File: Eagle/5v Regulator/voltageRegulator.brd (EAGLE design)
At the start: 49 x 43 mm, 9 parts, among them U1 LM2576HVS-5.0/NOPB

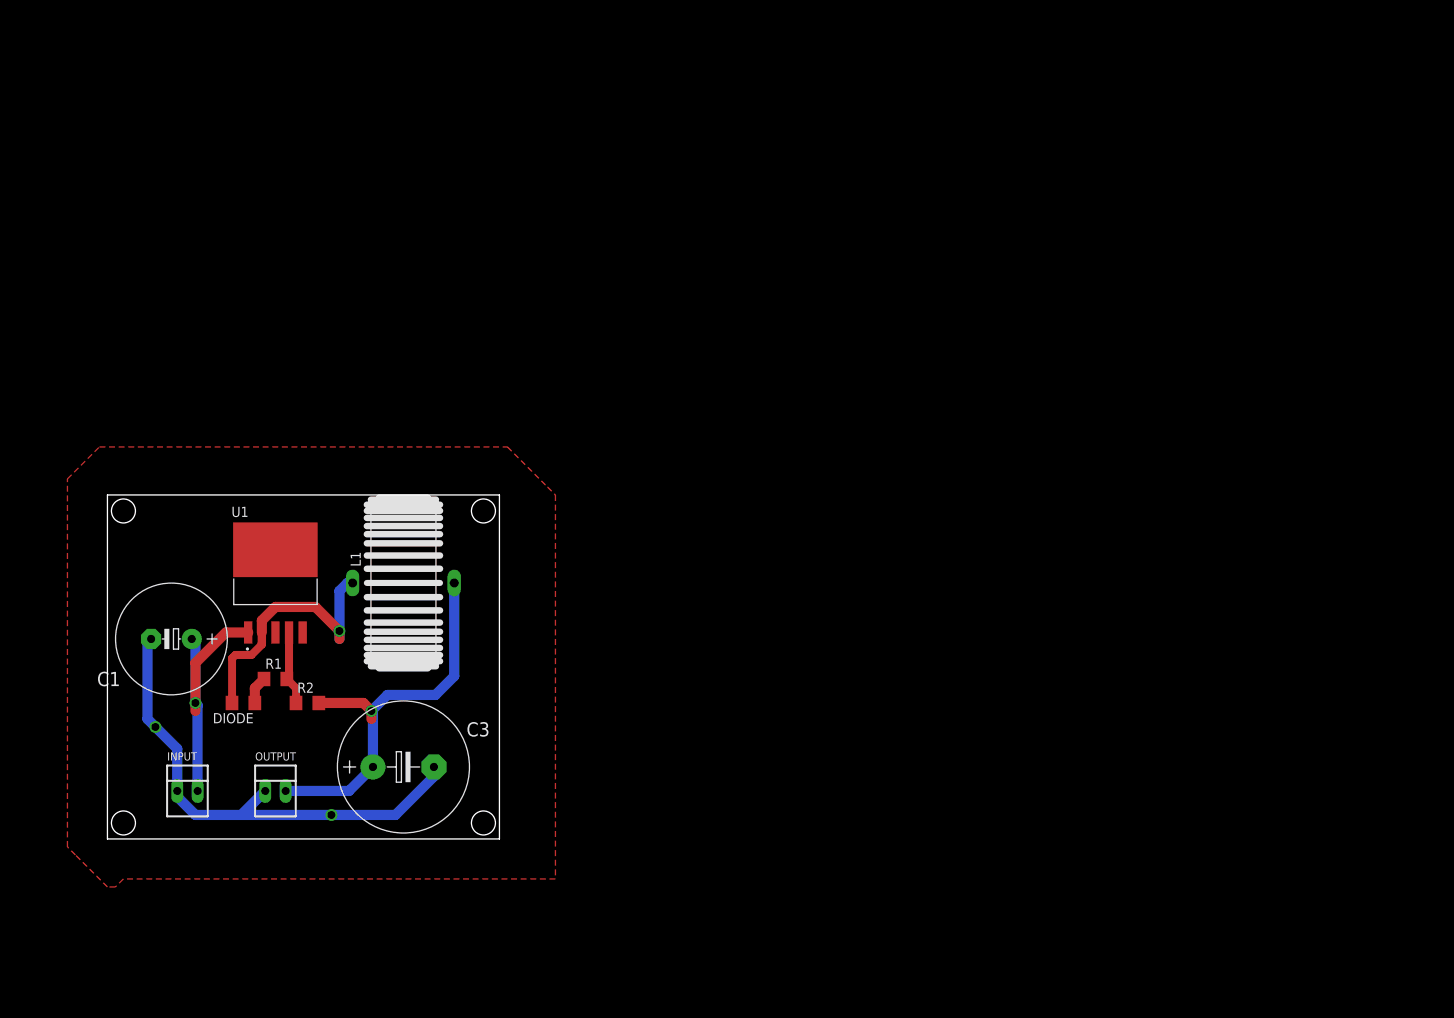
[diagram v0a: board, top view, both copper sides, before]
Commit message: Updated the voltage regulator board
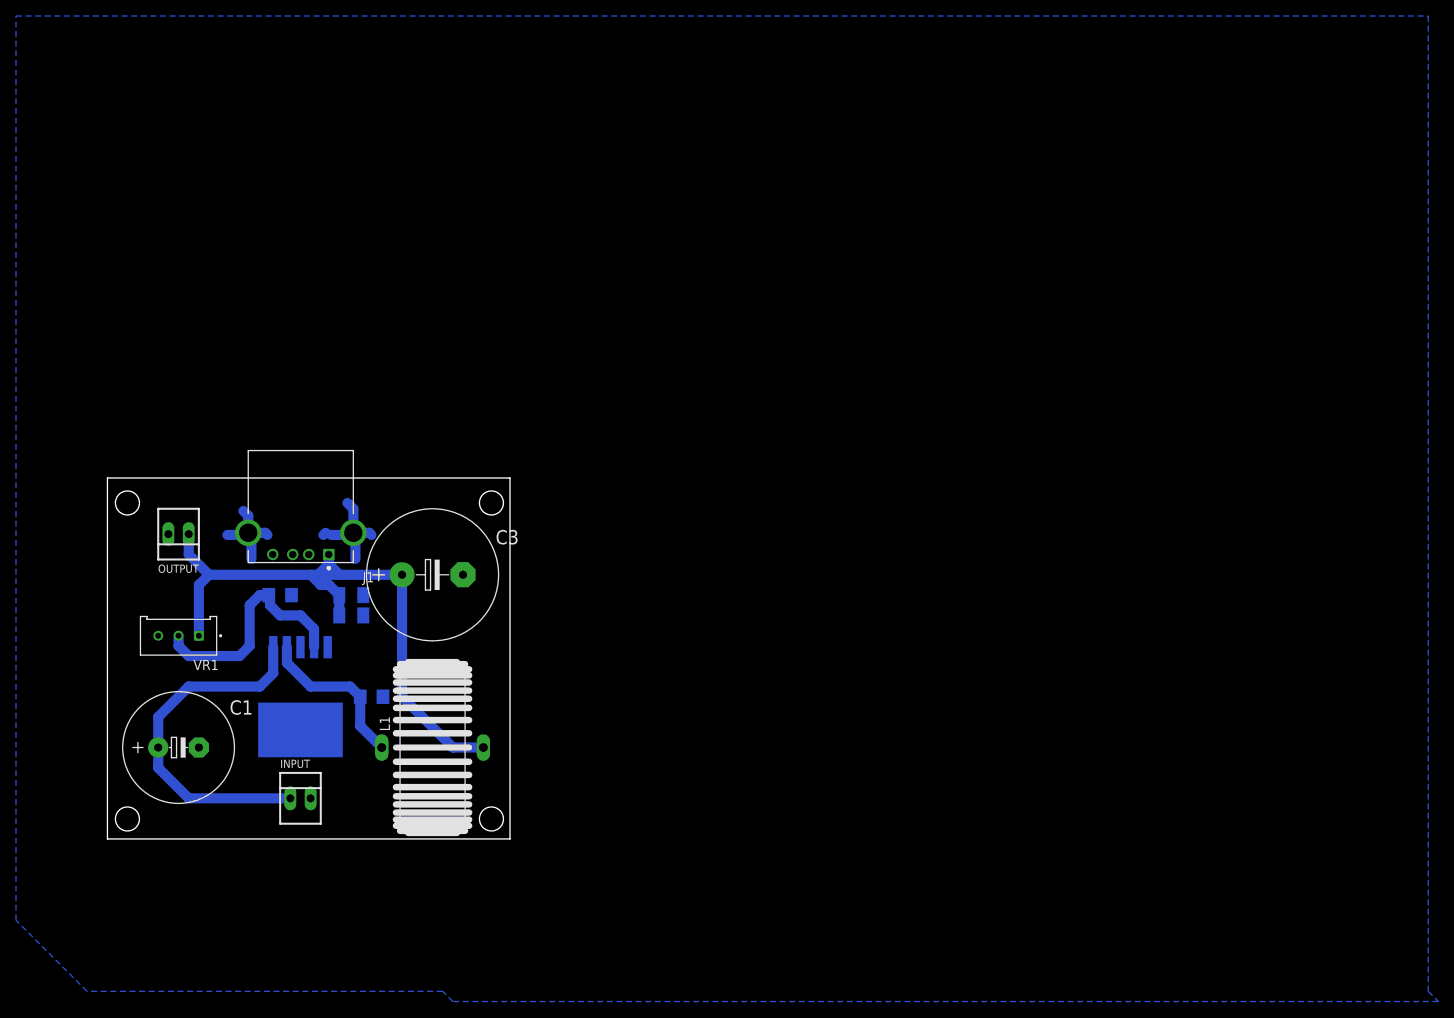
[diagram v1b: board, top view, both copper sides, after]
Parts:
- removed R2: 3000, rcl:R1206
- added C2, C4: (no value), rcl:C1206K
- added J1: 292303-1, 292303-1:TE_292303-1
- added VR1: 3296W-1-250, 3296W-1-250:TRIM_3296W-1-250
- moved OUTPUT 34.3 mm to (8.89, 38.1), turned to 180 degrees
- moved C3 24.3 mm to (40.6, 33.0)
- moved L1 20.9 mm to (40.6, 11.4)
- moved DIODE 16.0 mm to (33.0, 17.8), flipped to the bottom, turned to 0 degrees
- moved U1 14.6 mm to (24.1, 17.8), flipped to the bottom, turned to 180 degrees
- moved INPUT 14.2 mm to (24.1, 5.08)
- moved C1 13.6 mm to (8.89, 11.4), turned to 0 degrees
- moved R1 10.5 mm to (21.6, 30.5), flipped to the bottom
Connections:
- net FEEDBACK: now also VR1.2; no longer R2.1
- net GND: now also C2.1, C4.2, INPUT.2, J1.4, J1.SH1, J1.SH2, OUTPUT.2, VR1.3; no longer INPUT.1, OUTPUT.1
- net LOAD+: now also C2.2, C4.1, J1.1, OUTPUT.1, VR1.1; no longer OUTPUT.2, R2.2
- net VCC: now also INPUT.1; no longer INPUT.2
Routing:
- net GND: track 65.4 -> 24.7 mm, vias 2 -> 0
- net LOAD+: track 50.8 -> 80.5 mm, vias 1 -> 0
- net FEEDBACK: track 9.40 -> 29.5 mm
- net OUTPUT: track 33.7 -> 20.3 mm, vias 1 -> 0
- net VCC: track 33.5 -> 44.3 mm, vias 1 -> 0
- added copper zone on layer 16, net GND
- removed copper zone on layer 1, net GND
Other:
- board size 49 x 43 mm -> 50.3 x 45.1 mm
